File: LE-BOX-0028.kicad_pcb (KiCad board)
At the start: 2 copper layers, 76 x 96 mm, 65 parts, among them P1 MYSX_1.5, P2 CONN_02X03, P3 CONN_01X03, P4 CONN_01X03, Q1 DMP3056L-7, Q2 DMP3056L-7, U1 LD1117DT33TR, U2 TPS61097A, U3 ATSHA204A, U4 RFM69HW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

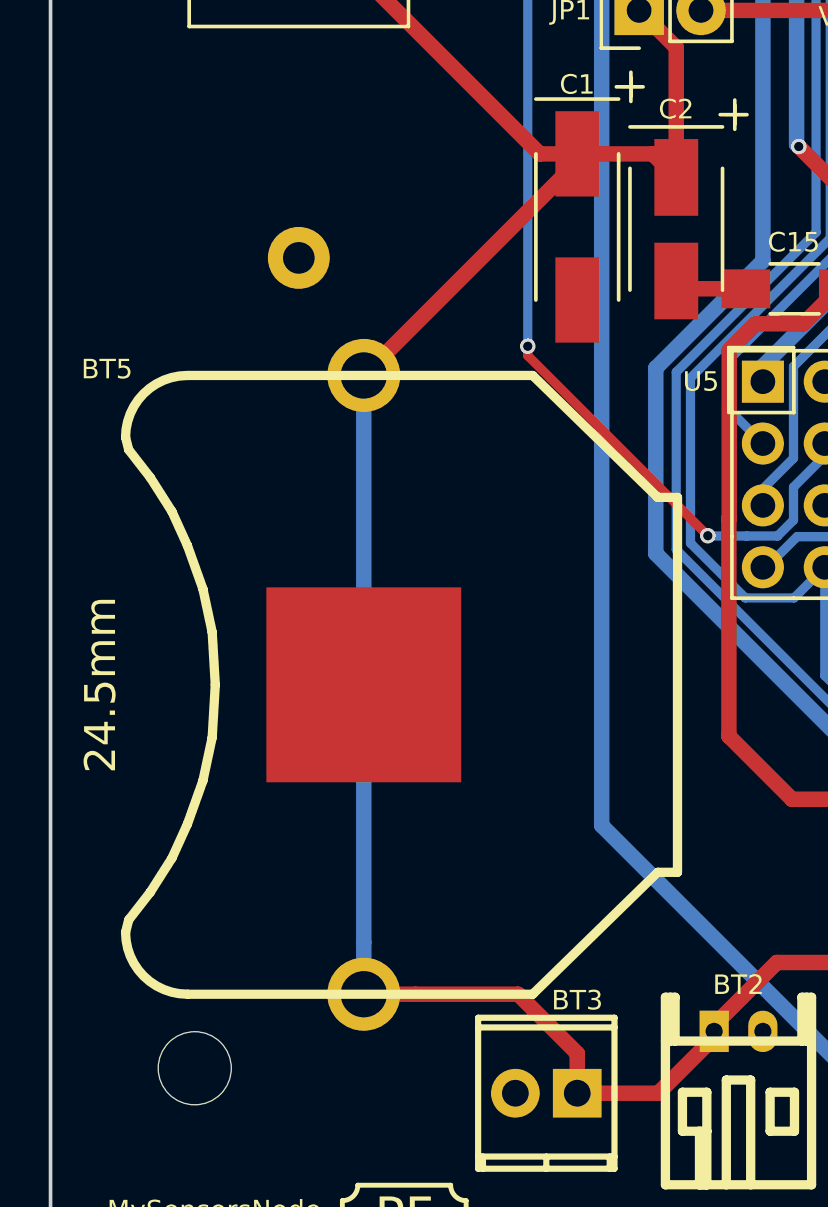
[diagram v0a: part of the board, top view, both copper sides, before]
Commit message: Moved BT5 to make more room for mounting screw
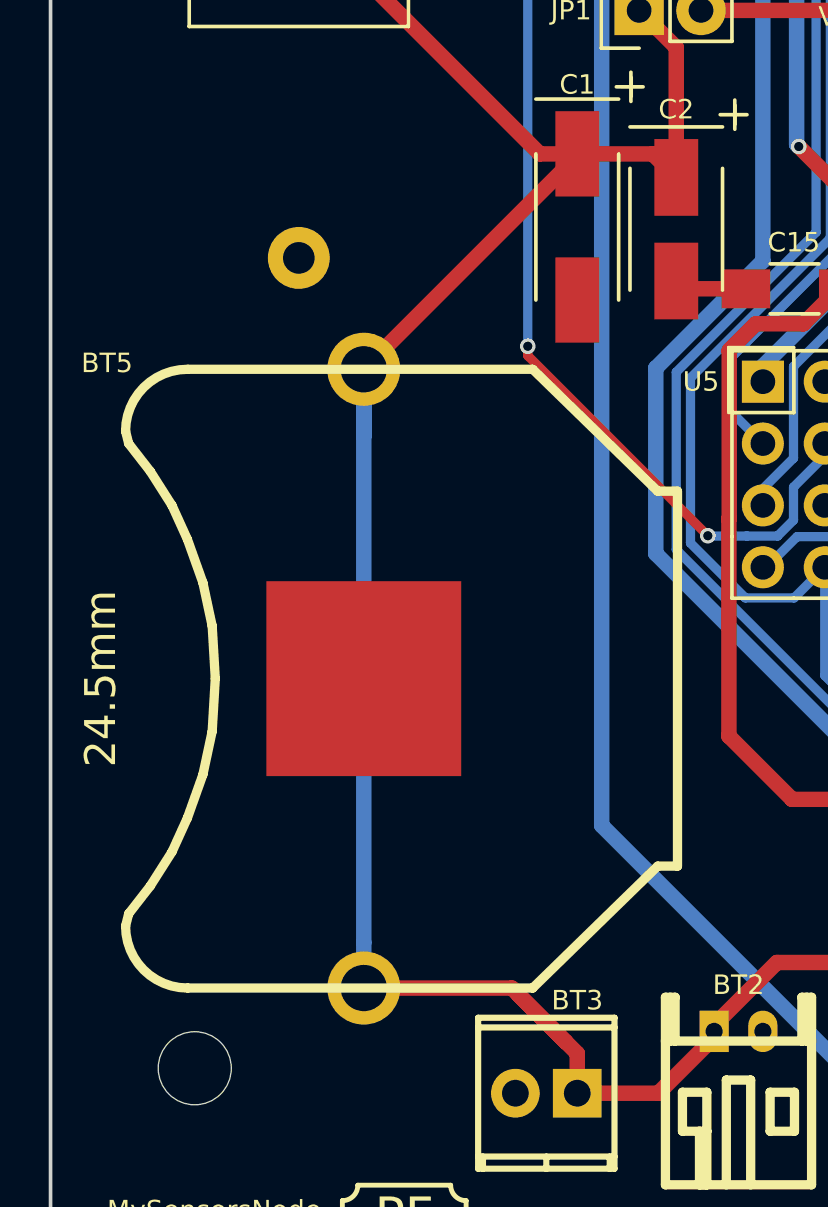
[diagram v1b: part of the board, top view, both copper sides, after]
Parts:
- moved BT5 0.25 mm to (100.6, 122.6)
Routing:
- net Net-(BT1-Pad3): track 119.2 -> 124.6 mm
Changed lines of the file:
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@@
   (general
     (links 180)
-    (no_connects 2)
-    (area 87.704196 51.910252 163.854198 148.060254)
+    (no_connects 0)
+    (area 80.161001 49.4806 167.066729 150.1516)
     (thickness 1.2)
     (drawings 41)
-    (tracks 1765)
+    (tracks 1768)
     (zones 0)
     (modules 65)
@@
     (44 Edge.Cuts user)
     (46 B.CrtYd user hide)
-    (47 F.CrtYd user hide)
+    (47 F.CrtYd user)
   )
   (setup
@@
   )
   (module mysensors_connectors:keystone_3009-kcswalter locked (layer F.Cu)
-    (at 100.638 122.8466 270)
+    (at 100.638 122.5926 270)
     (descr "Keystone type 3009 coin cell retainer")
     (fp_text reference BT5 (at -12.954 10.541 360) (layer F.SilkS)
@@
   (segment (start 160.201 107.2766) (end 160.137 107.3406) (width 0.381) (layer F.Cu) (net 2))
   (segment (start 160.137 107.3406) (end 160.137 108.6406) (width 0.381) (layer F.Cu) (net 2))
+  (segment (start 100.638 109.8926) (end 109.401 101.1296) (width 0.635) (layer F.Cu) (net 3))
+  (segment (start 109.401 101.1296) (end 109.401 101.05086) (width 0.635) (layer F.Cu) (net 3))
+  (segment (start 100.638 112.632154) (end 100.638 110.1466) (width 0.635) (layer B.Cu) (net 3))
+  (segment (start 100.638 133.42528) (end 100.638 112.632154) (width 0.635) (layer B.Cu) (net 3))
+  (segment (start 100.638 112.632154) (end 100.638 109.8926) (width 0.635) (layer B.Cu) (net 3))
+  (segment (start 109.401 137.97611) (end 108.931505 137.506615) (width 0.635) (layer F.Cu) (net 3))
+  (segment (start 108.931505 137.506615) (end 106.97149 135.5466) (width 0.635) (layer F.Cu) (net 3))
+  (segment (start 100.638 135.2926) (end 106.71749 135.2926) (width 0.635) (layer F.Cu) (net 3))
+  (segment (start 106.71749 135.2926) (end 108.931505 137.506615) (width 0.635) (layer F.Cu) (net 3))
   (segment (start 100.638 135.5466) (end 100.638 133.42528) (width 0.635) (layer B.Cu) (net 3))
-  (segment (start 100.638 133.42528) (end 100.638 110.1466) (width 0.635) (layer B.Cu) (net 3))
   (segment (start 113.465 102.0186) (end 113.465 96.6846) (width 0.635) (layer F.Cu) (net 3))
   (segment (start 113.465 96.6846) (end 111.941 95.1606) (width 0.635) (layer F.Cu) (net 3))
   (segment (start 109.401 101.05086) (end 112.49726 101.05086) (width 0.635) (layer F.Cu) (net 3))
   (segment (start 112.49726 101.05086) (end 113.465 102.0186) (width 0.635) (layer F.Cu) (net 3))
-  (segment (start 100.638 110.1466) (end 109.401 101.3836) (width 0.635) (layer F.Cu) (net 3))
-  (segment (start 109.401 101.3836) (end 109.401 101.05086) (width 0.635) (layer F.Cu) (net 3))
   (segment (start 97.971 67.8206) (end 97.971 91.15629) (width 0.635) (layer F.Cu) (net 3))
   (segment (start 97.971 91.15629) (end 107.86557 101.05086) (width 0.635) (layer F.Cu) (net 3))
   (segment (start 107.86557 101.05086) (end 109.401 101.05086) (width 0.635) (layer F.Cu) (net 3))
   (segment (start 109.401 139.6106) (end 109.401 137.97611) (width 0.635) (layer F.Cu) (net 3))
-  (segment (start 109.401 137.97611) (end 106.97149 135.5466) (width 0.635) (layer F.Cu) (net 3))
-  (segment (start 106.97149 135.5466) (end 102.75932 135.5466) (width 0.635) (layer F.Cu) (net 3))
-  (segment (start 102.75932 135.5466) (end 100.638 135.5466) (width 0.635) (layer F.Cu) (net 3))
   (segment (start 109.401 139.6106) (end 112.72967 139.6106) (width 0.635) (layer F.Cu) (net 3))
   (segment (start 112.72967 139.6106) (end 115.01948 137.32079) (width 0.635) (layer F.Cu) (net 3))

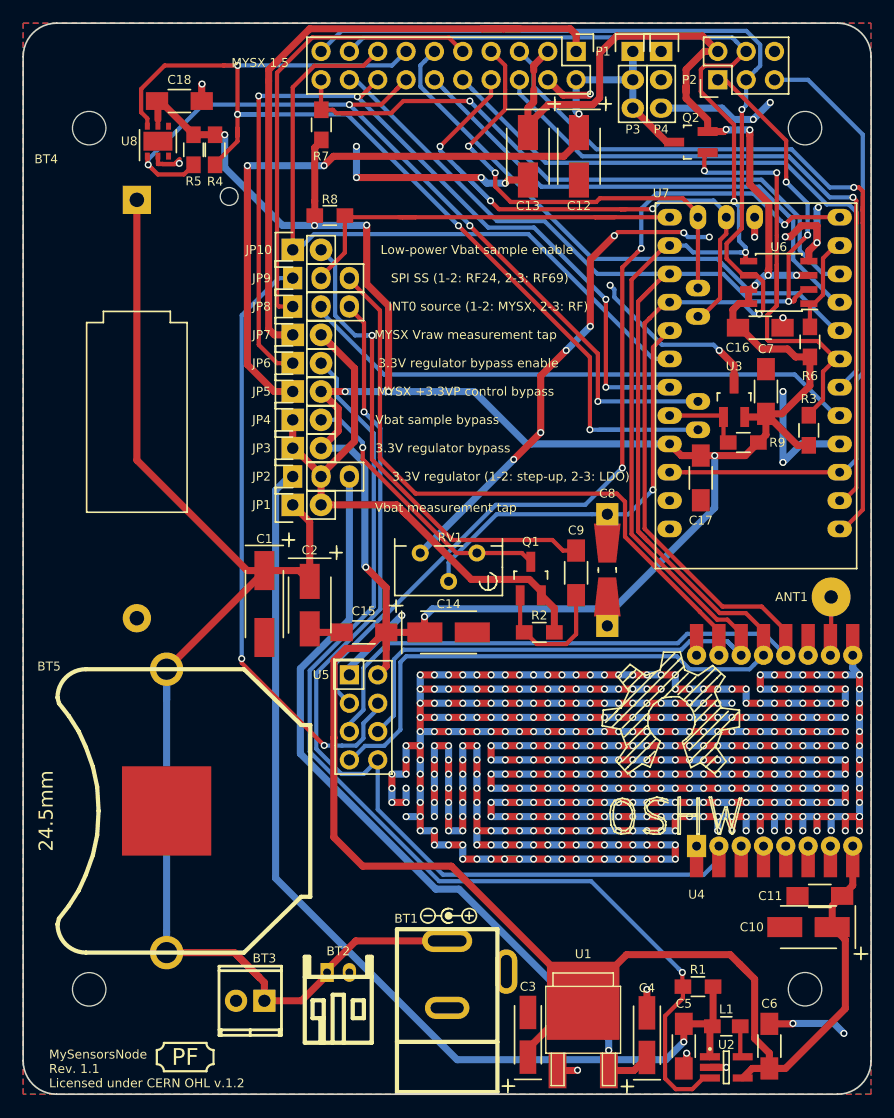
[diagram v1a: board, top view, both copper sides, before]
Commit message: Added a step-up reg and some sourcing details
Added TI TPS61221 (3.3V fixed) as an alternative to TPS61097A.
Also added some more sourcing details to some components in the
schematic.
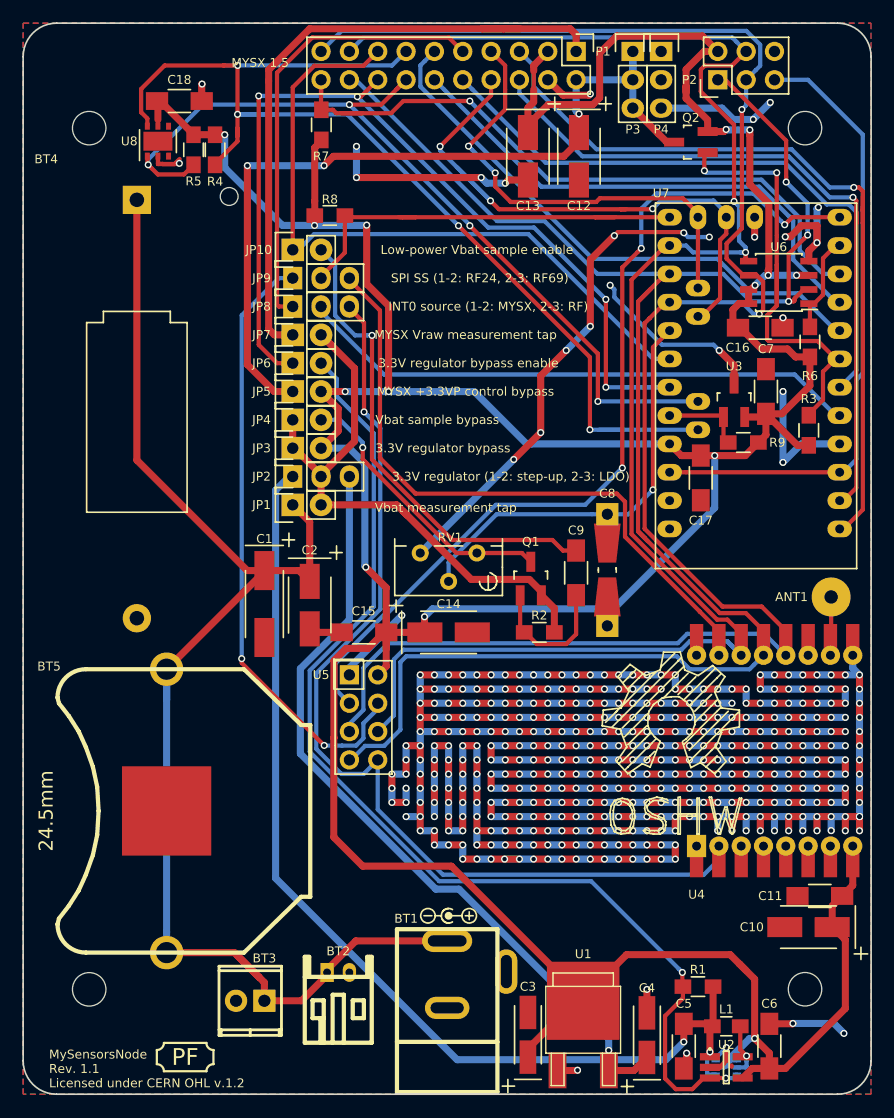
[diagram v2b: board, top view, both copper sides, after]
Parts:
- added U9: TPS6122X, Housings_SOT-23_SOT-143_TSOT-6:SC-70-6, B.Cu at (150.8, 145.6)
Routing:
- net +3V3: track 375.3 -> 381.3 mm, vias 13 -> 14
- net GND: track 688.9 -> 693.3 mm
- net Net-(C5-Pad1): track 91.5 -> 94.4 mm, vias 1 -> 2
- net Net-(JP6-Pad2): track 95.8 -> 98.3 mm, vias 1 -> 2
- net Net-(L1-Pad1): track 2.82 -> 5.09 mm, vias 0 -> 1

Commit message: Updated CR123 battery holder footprint
Fixes #11
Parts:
- U9: value TPS6122X -> TPS61221
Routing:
- net GND: track 693.3 -> 718.6 mm, vias 453 -> 459
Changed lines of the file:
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@@
-(kicad_pcb (version 4) (host pcbnew "(2015-07-30 BZR 6023, Git cb629e0)-product")
+(kicad_pcb (version 4) (host pcbnew 0.201509101502+6177~30~ubuntu14.04.1-product)
   (general
     (links 186)
@@
     (thickness 1.2)
     (drawings 41)
-    (tracks 1803)
+    (tracks 1822)
     (zones 0)
     (modules 66)
@@
     )
   )
-  (module mysensors_connectors:CR123_holder locked (layer F.Cu)
-    (at 97.971 67.8206)
-    (descr "CR123 battery holder")
-    (tags "Battery holder, CR123")
-    (fp_text reference BT4 (at -8.128 -3.648) (layer F.SilkS)
-      (effects (font (size 0.8 0.8) (thickness 0.16)))
-    )
-    (fp_text value CR123 (at 0 2.54) (layer F.Fab)
-      (effects (font (size 1 1) (thickness 0.15)))
-    )
-    (fp_line (start -4.5 28) (end 4.5 28) (layer F.SilkS) (width 0.15))
-    (fp_line (start 4.5 28) (end 4.5 11) (layer F.SilkS) (width 0.15))
-    (fp_line (start 4.5 11) (end 3 11) (layer F.SilkS) (width 0.15))
-    (fp_line (start 3 11) (end 3 10) (layer F.SilkS) (width 0.15))
-    (fp_line (start 3 10) (end -3 10) (layer F.SilkS) (width 0.15))
-    (fp_line (start -3 10) (end -3 11) (layer F.SilkS) (width 0.15))
-    (fp_line (start -3 11) (end -4.5 11) (layer F.SilkS) (width 0.15))
-    (fp_line (start -4.5 11) (end -4.5 28) (layer F.SilkS) (width 0.15))
-    (fp_line (start -9.25 -2.75) (end 9.25 -2.75) (layer F.CrtYd) (width 0.15))
-    (fp_line (start 9.25 -2.75) (end 9.25 40.25) (layer F.CrtYd) (width 0.15))
-    (fp_line (start -9.25 40.25) (end 9.25 40.25) (layer F.CrtYd) (width 0.15))
-    (fp_line (start -9.25 -2.75) (end -9.25 40.25) (layer F.CrtYd) (width 0.15))
-    (pad 1 thru_hole rect (at 0 0) (size 2.54 2.54) (drill 1.3) (layers *.Cu *.Mask F.SilkS)
-      (net 3 "Net-(BT1-Pad3)"))
-    (pad 2 thru_hole circle (at 0 37.5) (size 2.54 2.54) (drill 1.3) (layers *.Cu *.Mask F.SilkS)
-      (net 1 GND))
-    (pad "" np_thru_hole circle (at 8.275 -0.3) (size 1.6 1.6) (drill 1.6) (layers *.Cu Dwgs.User))
-    (model mysensors.3dshapes/cr123_holder.wrl
-      (at (xyz 0 -0.737 0.28))
-      (scale (xyz 1 1 1))
-      (rotate (xyz 0 0 0))
-    )
-    (model Pin_Headers.3dshapes/Pin_Header_Straight_1x01.wrl
-      (at (xyz 0 0 0))
-      (scale (xyz 1 1 1))
-      (rotate (xyz 0 0 0))
-    )
-    (model Pin_Headers.3dshapes/Pin_Header_Straight_1x01.wrl
-      (at (xyz 0 -1.475 0))
-      (scale (xyz 1 1 1))
-      (rotate (xyz 0 0 0))
-    )
-  )
   (module mysensors_connectors:keystone_3009-kcswalter locked (layer F.Cu)
     (at 100.638 122.5926 270)
@@
       (effects (font (size 0.8 0.8) (thickness 0.16)) (justify mirror))
     )
-    (fp_text value TPS6122X (at 0.04064 -4.191 90) (layer B.Fab)
+    (fp_text value TPS61221 (at 0.04064 -4.191 90) (layer B.Fab)
       (effects (font (size 1 1) (thickness 0.15)) (justify mirror))
     )
@@
     )
   )
+  (module mysensors_connectors:CR123_holder (layer F.Cu)
+    (at 97.971 67.8206)
+    (descr "CR123 battery holder")
+    (tags "Battery holder, CR123")
+    (fp_text reference BT4 (at 0 -3.5) (layer F.SilkS)
+      (effects (font (size 1 1) (thickness 0.15)))
+    )
+    (fp_text value CR123 (at 0 2.54) (layer F.Fab)
+      (effects (font (size 1 1) (thickness 0.15)))
+    )
+    (fp_line (start -4.5 28) (end 4.5 28) (layer F.SilkS) (width 0.15))
+    (fp_line (start 4.5 28) (end 4.5 11) (layer F.SilkS) (width 0.15))
+    (fp_line (start 4.5 11) (end 3 11) (layer F.SilkS) (width 0.15))
+    (fp_line (start 3 11) (end 3 10) (layer F.SilkS) (width 0.15))
+    (fp_line (start 3 10) (end -3 10) (layer F.SilkS) (width 0.15))
+    (fp_line (start -3 10) (end -3 11) (layer F.SilkS) (width 0.15))
+    (fp_line (start -3 11) (end -4.5 11) (layer F.SilkS) (width 0.15))
+    (fp_line (start -4.5 11) (end -4.5 28) (layer F.SilkS) (width 0.15))
+    (fp_line (start -9.25 -2.75) (end 9.25 -2.75) (layer F.CrtYd) (width 0.15))
+    (fp_line (start 9.25 -2.75) (end 9.25 40.25) (layer F.CrtYd) (width 0.15))
+    (fp_line (start -9.25 40.25) (end 9.25 40.25) (layer F.CrtYd) (width 0.15))
+    (fp_line (start -9.25 -2.75) (end -9.25 40.25) (layer F.CrtYd) (width 0.15))
+    (pad 1 thru_hole rect (at 0 0) (size 2.54 2.54) (drill 1.3) (layers *.Cu *.Mask F.SilkS)
+      (net 3 "Net-(BT1-Pad3)"))
+    (pad 2 thru_hole circle (at 0 37.82) (size 2.54 2.54) (drill 1.3) (layers *.Cu *.Mask F.SilkS)
+      (net 1 GND))
+    (pad "" np_thru_hole circle (at 8.1 0) (size 1.98 1.98) (drill 1.98) (layers *.Cu Dwgs.User))
+    (model mysensors.3dshapes/cr123_holder.wrl
+      (at (xyz 0 -0.746 0.28))
+      (scale (xyz 1 1 1))
+      (rotate (xyz 0 0 0))
+    )
+    (model Pin_Headers.3dshapes/Pin_Header_Straight_1x01.wrl
+      (at (xyz 0 0 0))
+      (scale (xyz 1 1 1))
+      (rotate (xyz 0 0 0))
+    )
+    (model Pin_Headers.3dshapes/Pin_Header_Straight_1x01.wrl
+      (at (xyz 0 -1.49 0))
+      (scale (xyz 1 1 1))
+      (rotate (xyz 0 0 0))
+    )
+  )
   (gr_text "MYSX +3.3VP control bypass" (at 127.435 85.0006) (layer F.SilkS)
     (effects (font (size 0.8 0.8) (thickness 0.16)))
@@
   )
   (segment (start 151.2856 145.5288) (end 151.2856 145.4018) (width 0.381) (layer F.Cu) (net 0))
+  (segment (start 153.67 136.017) (end 153.67 137.033) (width 0.635) (layer B.Cu) (net 1))
+  (segment (start 153.67 137.033) (end 151.765 138.938) (width 0.635) (layer B.Cu) (net 1))
+  (via (at 151.765 138.938) (size 0.635) (drill 0.381) (layers F.Cu B.Cu) (net 1))
+  (segment (start 154.6638 141.6746) (end 154.6638 137.0108) (width 0.635) (layer F.Cu) (net 1))
+  (segment (start 154.6638 137.0108) (end 153.67 136.017) (width 0.635) (layer F.Cu) (net 1))
+  (via (at 153.67 136.017) (size 0.635) (drill 0.381) (layers F.Cu B.Cu) (net 1))
+  (segment (start 131.064 97.155) (end 131.064 100.203) (width 0.635) (layer B.Cu) (net 1))
+  (segment (start 131.064 100.203) (end 130.683 100.584) (width 0.635) (layer B.Cu) (net 1))
+  (via (at 130.683 100.584) (size 0.635) (drill 0.381) (layers F.Cu B.Cu) (net 1))
+  (segment (start 127.353808 95.495792) (end 129.404792 95.495792) (width 0.635) (layer F.Cu) (net 1))
+  (segment (start 129.404792 95.495792) (end 131.064 97.155) (width 0.635) (layer F.Cu) (net 1))
+  (via (at 131.064 97.155) (size 0.635) (drill 0.381) (layers F.Cu B.Cu) (net 1))
+  (segment (start 123.371 99.4786) (end 127.353808 95.495792) (width 0.635) (layer B.Cu) (net 1))
+  (segment (start 127.353808 95.495792) (end 131.753 91.0966) (width 0.635) (layer B.Cu) (net 1))
+  (segment (start 127.508 93.091) (end 127.508 95.3416) (width 0.635) (layer B.Cu) (net 1))
+  (via (at 127.353808 95.495792) (size 0.635) (drill 0.381) (layers F.Cu B.Cu) (net 1))
+  (segment (start 127.508 95.3416) (end 127.353808 95.495792) (width 0.635) (layer B.Cu) (net 1))
+  (segment (start 131.753 91.0966) (end 129.5024 91.0966) (width 0.635) (layer F.Cu) (net 1))
+  (segment (start 129.5024 91.0966) (end 127.508 93.091) (width 0.635) (layer F.Cu) (net 1))
+  (via (at 127.508 93.091) (size 0.635) (drill 0.381) (layers F.Cu B.Cu) (net 1))
   (segment (start 150.803 144.986361) (end 150.209761 145.5796) (width 0.381) (layer F.Cu) (net 1))
   (segment (start 150.803 143.8016) (end 150.803 144.986361) (width 0.381) (layer F.Cu) (net 1))
@@
   (segment (start 131.753 91.0966) (end 134.166 88.6836) (width 0.635) (layer F.Cu) (net 1))
   (via (at 134.166 88.6836) (size 0.635) (drill 0.381) (layers F.Cu B.Cu) (net 1))
-  (segment (start 123.371 99.4786) (end 131.753 91.0966) (width 0.635) (layer B.Cu) (net 1))
   (via (at 131.753 91.0966) (size 0.635) (drill 0.381) (layers F.Cu B.Cu) (net 1))
   (segment (start 136.185301 58.444901) (end 138.496699 58.444901) (width 0.635) (layer F.Cu) (net 1))

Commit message: Minor layout beautifications
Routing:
- net GND: track 718.6 -> 717.4 mm, vias 459 -> 458
- net MYSX_3.3V_EN: track 40.5 -> 39.9 mm
